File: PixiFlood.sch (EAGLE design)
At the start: 31 parts, among them IC1 78L05Z, IC2 WS2811-SOP8, IC3 TC7W04FTC7W04F, U1 PT4115PT4115B89E, U2 PT4115PT4115B89E, U3 PT4115PT4115B89E, X1 22-23-2031, X2 LED-PAD, X3 LED-PAD, X4 22-23-2031, X5 LED-PAD, X6 LED-PAD, X7 LED-PAD, X8 LED-PAD

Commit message: Reworked and retitled to PixiFlood
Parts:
- D1, D2, D3: value (none) -> 1N5819
- IC2: value WS2811-SOP8 -> WS2811SOP8; device MyLibrary:WS2811-SOP8 -> drivers:WS2811SOP8
- IC3: value TC7W04FTC7W04F -> TC7W04F; device MyLibrary:TC7W04FTC7W04F -> logic:TC7W04F
- L1, L2, L3: value SLF7045 -> 82114R; device inductors:SLF7045 -> inductors:82114R
- R1, R6: device resistor:R-US_R1206 -> resistor:R-US_0204/5
- R2, R3, R4: device rcl:R-US_M0805 -> rcl:R-US_0204/5
- R5: device resistor:R-US_M1206 -> resistor:R-US_0204/5
- U1, U2, U3: value PT4115PT4115B89E -> PT4115B89E; device IC:PT4115PT4115B89E -> drivers:PT4115B89E
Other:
- moved on the sheet: R1, R5, R6, X2, X3, X5, X6, X7, X8

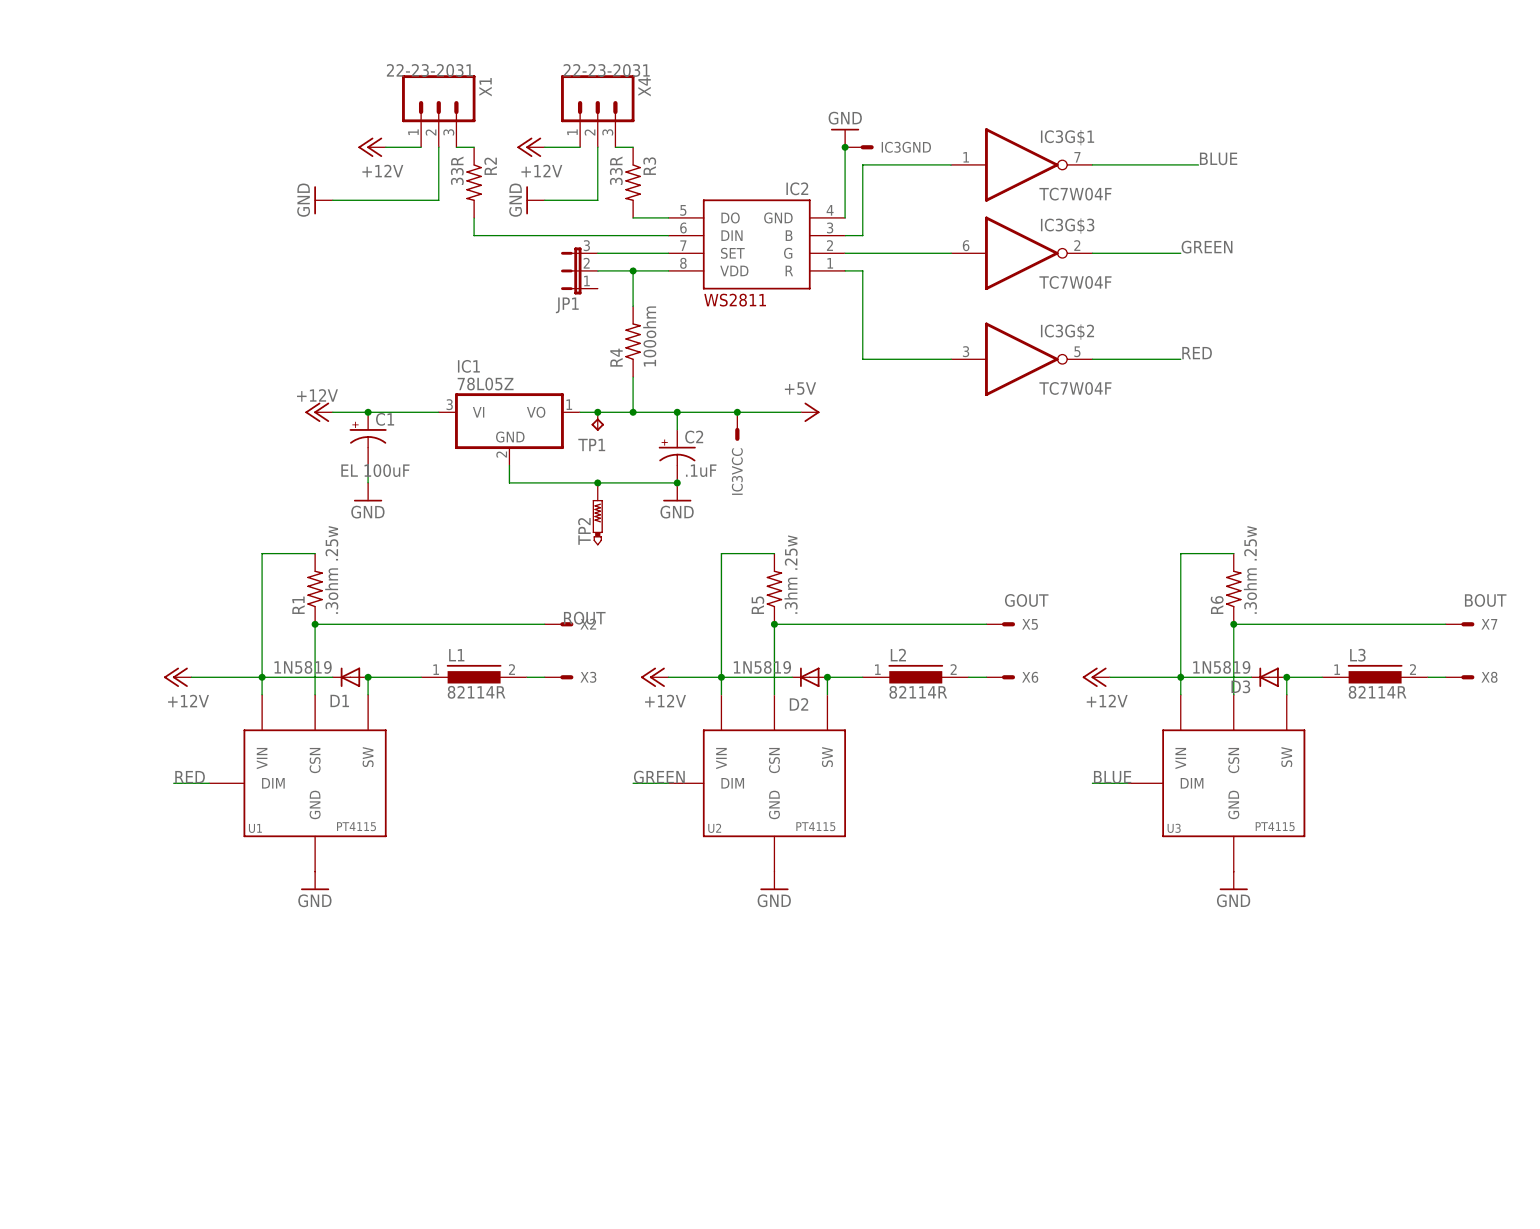
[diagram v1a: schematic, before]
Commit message: Reworked and retitled to PixiFlood SMD
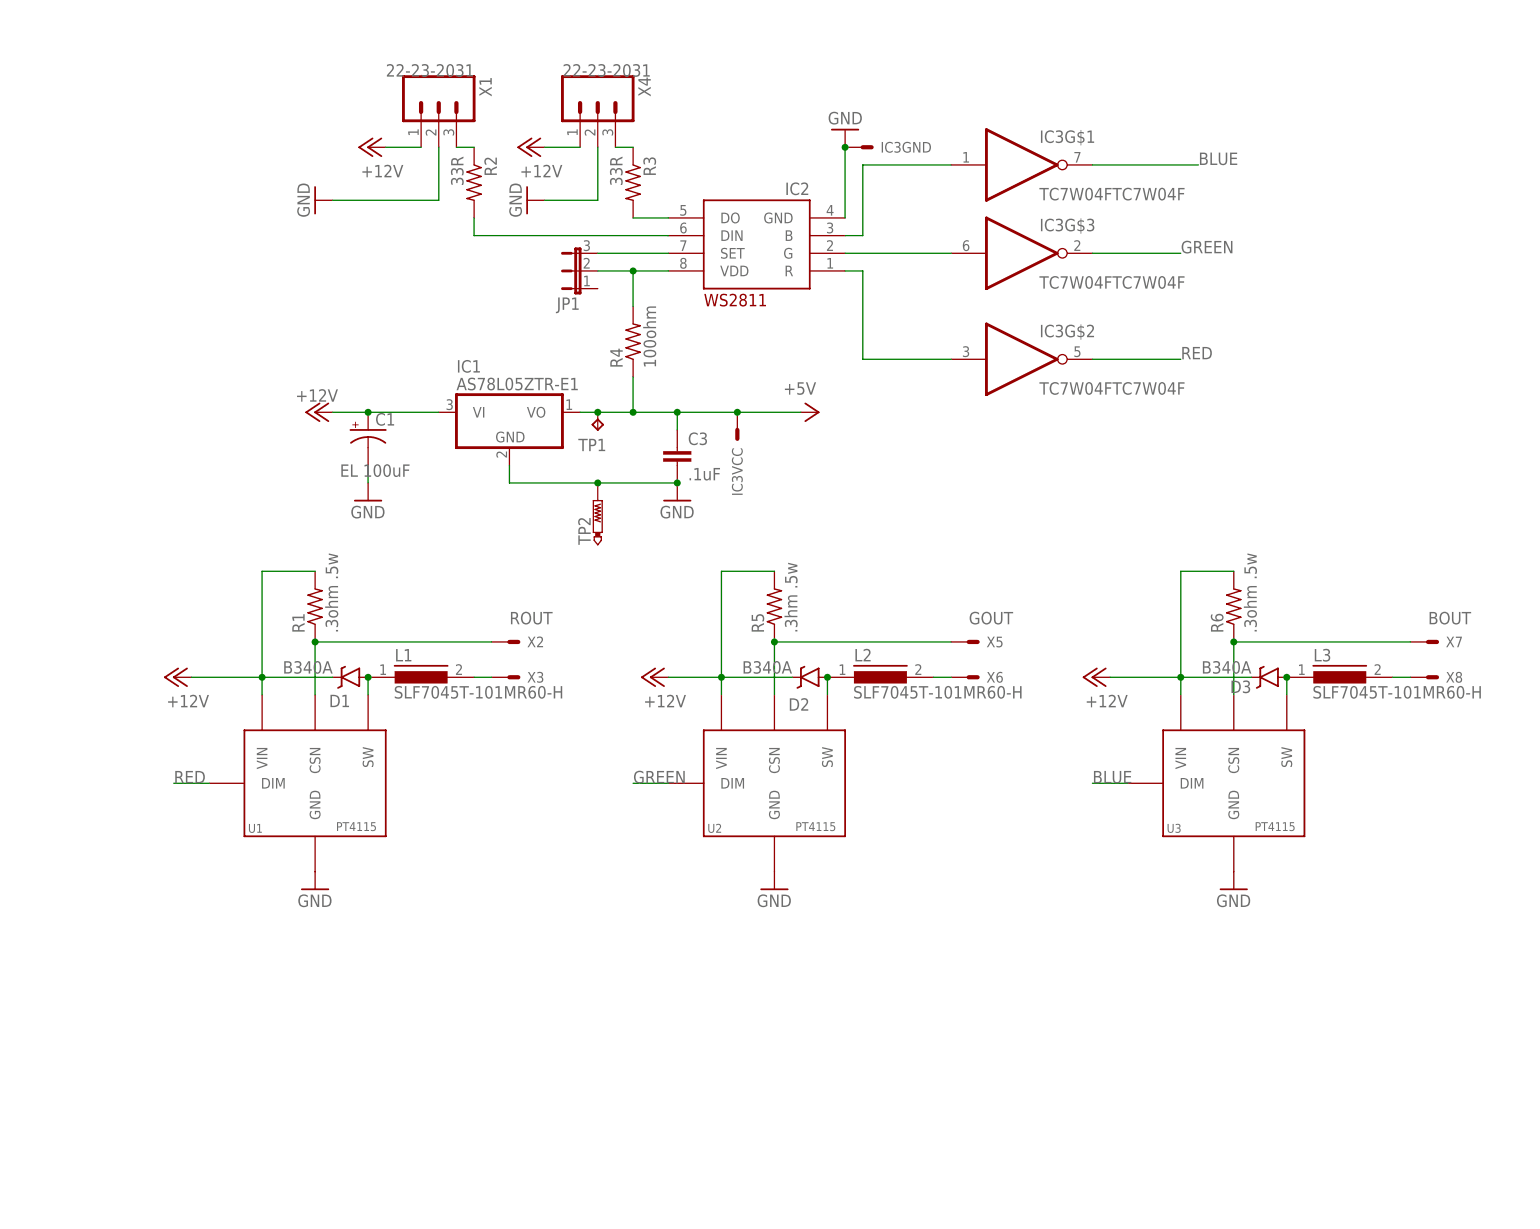
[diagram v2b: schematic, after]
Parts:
- removed C2: .1uF, resistor:CPOL-USB45181A
- added C3: .1uF, SparkFun-Capacitors:CAP1210
- D1, D2, D3: value 1N5819 -> B340A; device diode:DIODE-DO07 -> SparkFun-DiscreteSemi:DIODE-SCHOTTKY-B340A
- IC1: value 78L05Z -> AS78L05ZTR-E1
- IC2: value WS2811SOP8 -> WS2811-SOP8; device drivers:WS2811SOP8 -> MyLibrary:WS2811-SOP8
- IC3: value TC7W04F -> TC7W04FTC7W04F; device logic:TC7W04F -> MyLibrary:TC7W04FTC7W04F
- L1, L2, L3: value 82114R -> SLF7045T-101MR60-H; device inductors:82114R -> inductors:SLF7045
- R1, R6: value .3ohm .25w -> .3ohm .5w; device resistor:R-US_0204/5 -> resistor:R-US_R1210
- R2, R3, R4: device rcl:R-US_0204/5 -> rcl:R-US_R1206
- R5: value .3hm .25w -> .3hm .5w; device resistor:R-US_0204/5 -> resistor:R-US_R1210
- U1, U2, U3: value PT4115B89E -> PT4115PT4115B89E; device drivers:PT4115B89E -> IC:PT4115PT4115B89E
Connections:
- net +5V: now also C3.1; no longer C2.+
- net GND: now also C3.2; no longer C2.-
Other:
- moved on the sheet: R1, R5, R6, X2, X3, X5, X6, X7, X8

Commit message: Reworked layout
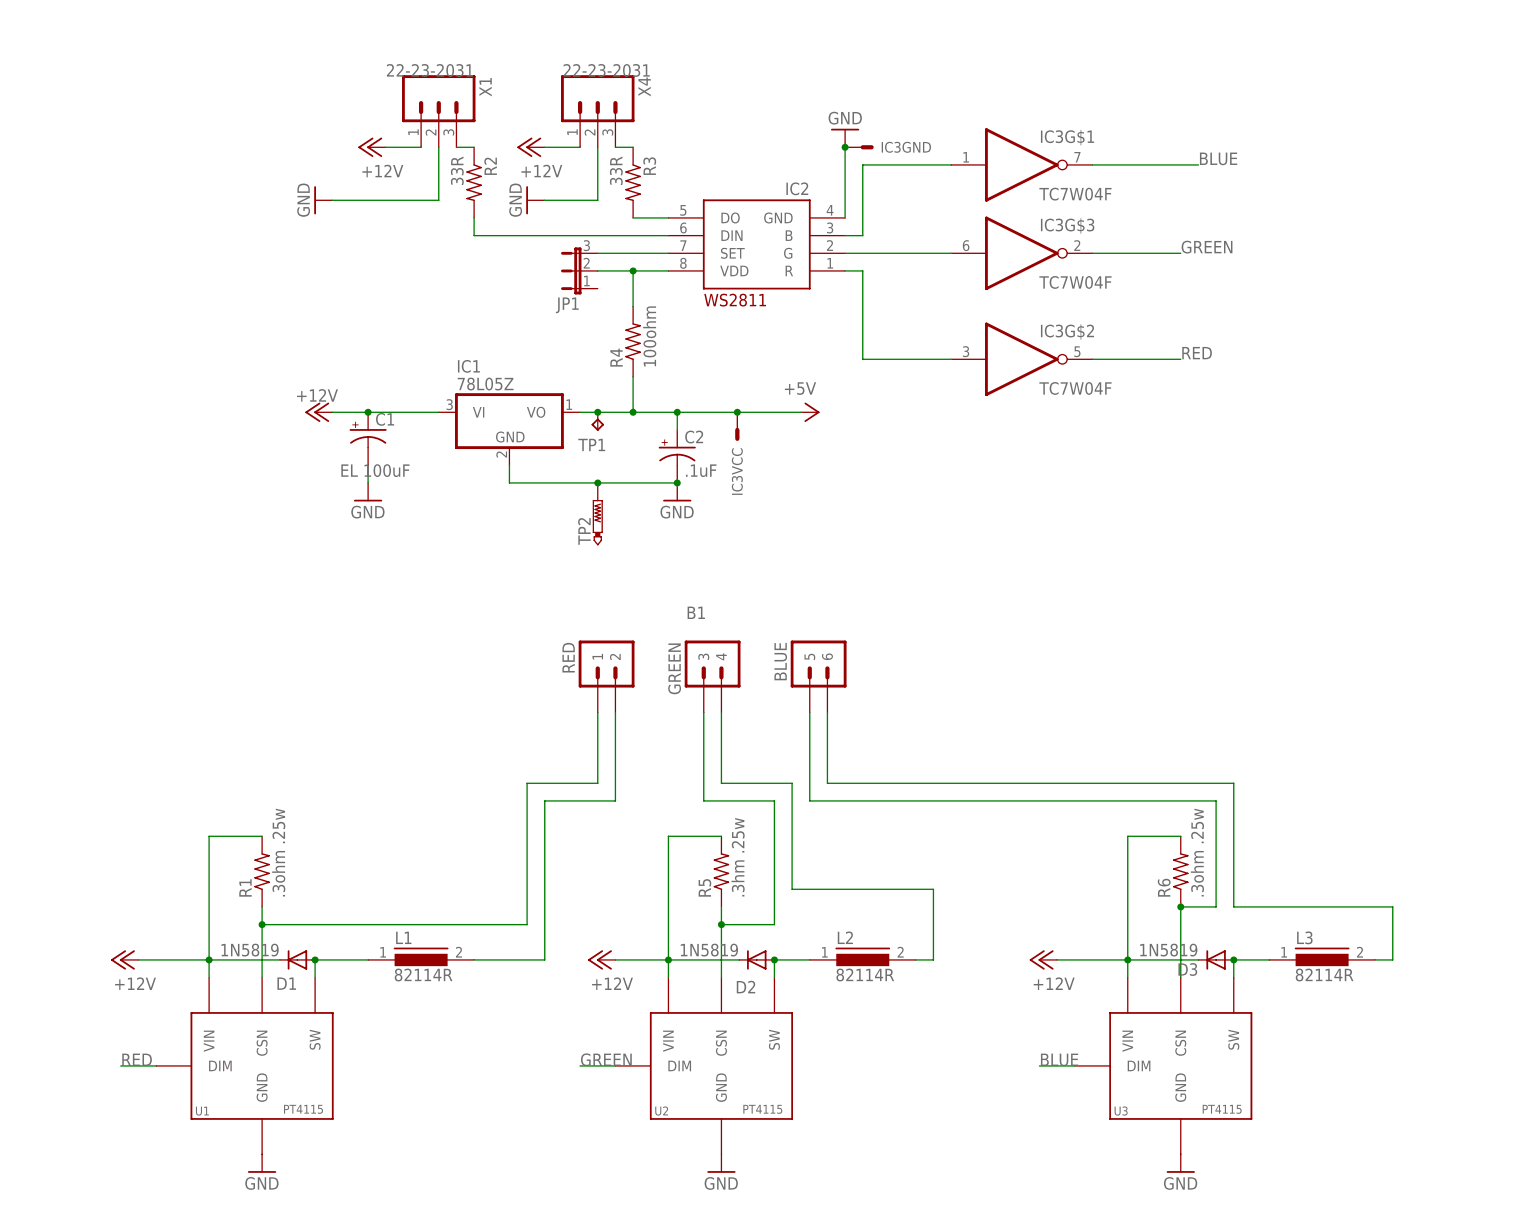
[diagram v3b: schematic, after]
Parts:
- removed C3: .1uF, SparkFun-Capacitors:CAP1210
- removed X2, X3, X5, X6, X7, X8: LED-PAD, MyLibrary:LED-PAD
- added B1: LED-BOARDV2, special:LED-BOARDV2
- added C2: .1uF, resistor:CPOL-USB45181A
- D1, D2, D3: value B340A -> 1N5819; device SparkFun-DiscreteSemi:DIODE-SCHOTTKY-B340A -> diode:DIODE-DO07
- IC1: value AS78L05ZTR-E1 -> 78L05Z
- IC2: value WS2811-SOP8 -> WS2811SOP8; device MyLibrary:WS2811-SOP8 -> drivers:WS2811SOP8
- IC3: value TC7W04FTC7W04F -> TC7W04F; device MyLibrary:TC7W04FTC7W04F -> logic:TC7W04F
- L1, L2, L3: value SLF7045T-101MR60-H -> 82114R; device inductors:SLF7045 -> inductors:82114R
- R1, R6: value .3ohm .5w -> .3ohm .25w; device resistor:R-US_R1210 -> resistor:R-US_0204/5
- R2, R3, R4: device rcl:R-US_R1206 -> rcl:R-US_0204/5
- R5: value .3hm .5w -> .3hm .25w; device resistor:R-US_R1210 -> resistor:R-US_0204/5
- U1, U2, U3: value PT4115PT4115B89E -> PT4115B89E; device IC:PT4115PT4115B89E -> drivers:PT4115B89E
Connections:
- net +5V: now also C2.+; no longer C3.1
- net BOUT: now also B1.5; no longer X7.S
- net GND: now also C2.-; no longer C3.2
- net GOUT: now also B1.3; no longer X5.S
- net N$10: now also B1.6; no longer X8.S
- net N$3: now also B1.2; no longer X3.S
- net N$9: now also B1.4; no longer X6.S
- net ROUT: now also B1.1; no longer X2.S
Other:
- moved on the sheet: R1, R5, R6, U1, U2, U3

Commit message: Reworked layout
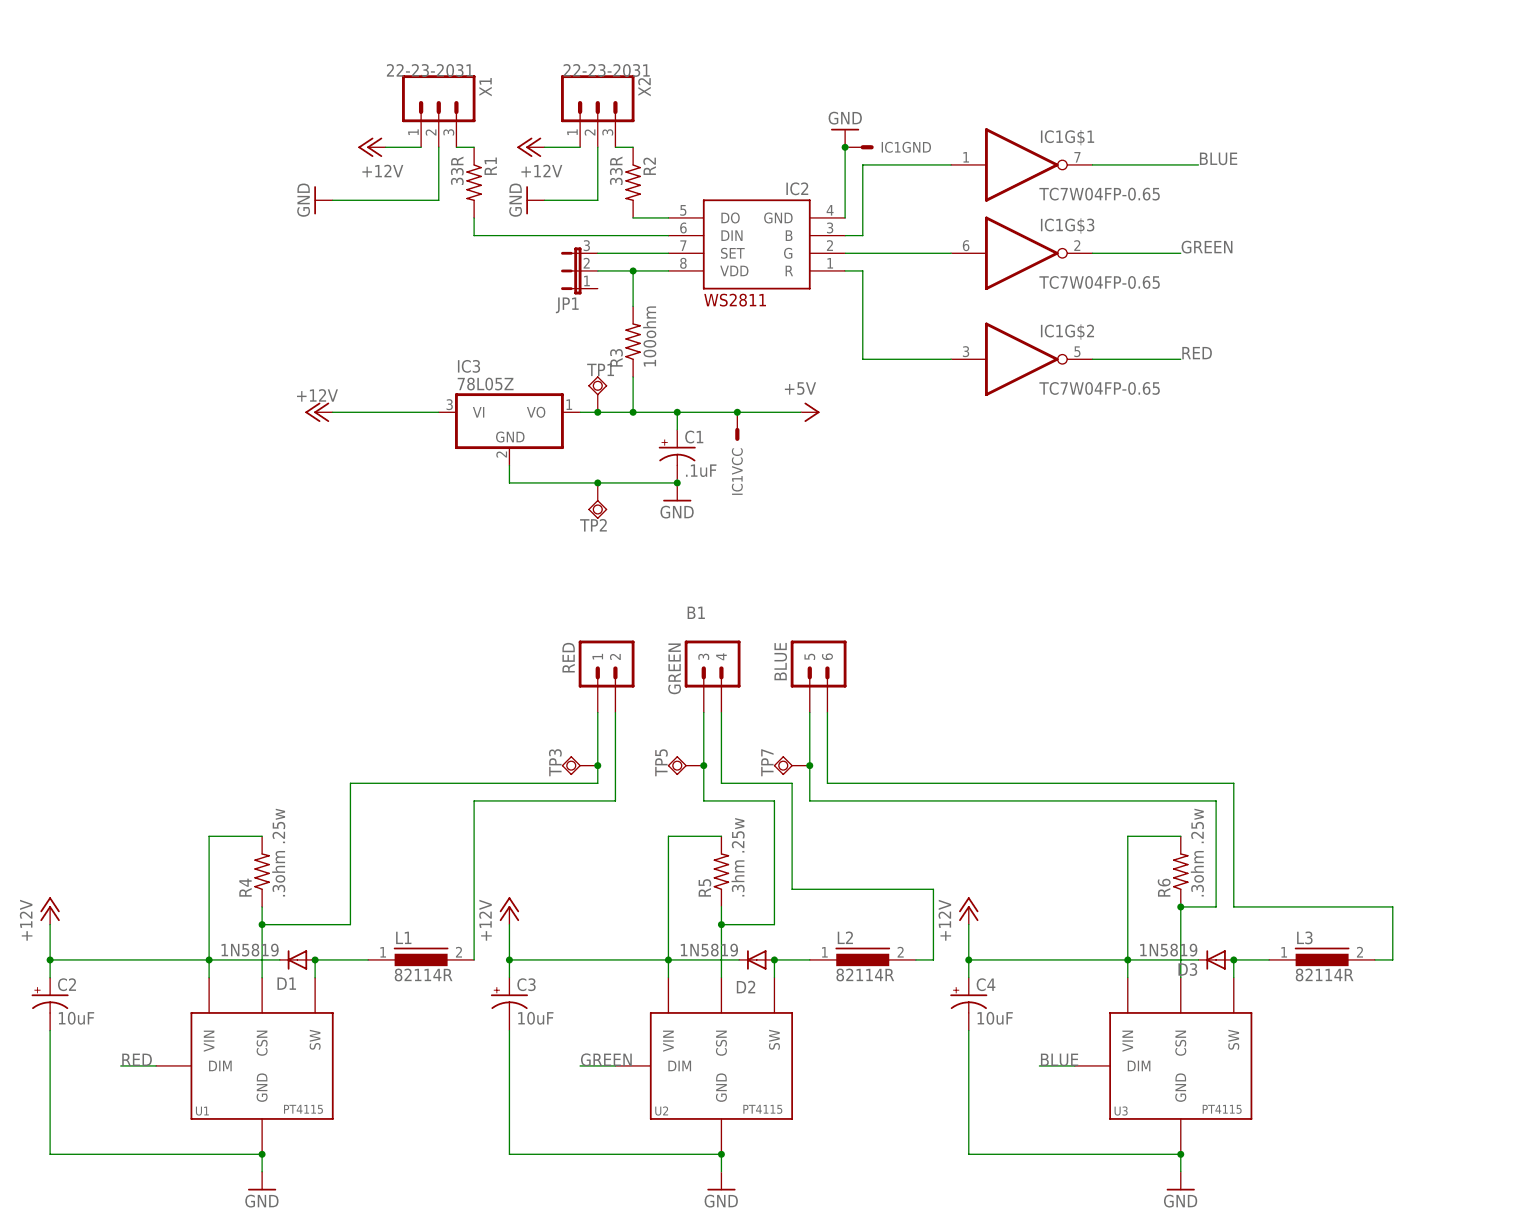
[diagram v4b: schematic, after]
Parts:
- added C3, C4: 10uF, adafruit:CPOL-USE2.5-5
- added TP3, TP5, TP7: TPSQTP15R, testpad:TPSQTP15R
- C1: value EL 100uF -> .1uF; device rcl:CPOL-USTT2D6L -> capacitors:CAP_POLPTH50
- C2: value .1uF -> 10uF; device resistor:CPOL-USB45181A -> adafruit:CPOL-USE2.5-5
- IC1: value 78L05Z -> TC7W04FP-0.65; device linear:78L05Z -> logic:TC7W04FP-0.65
- IC3: value TC7W04F -> 78L05Z; device logic:TC7W04F -> linear:78L05Z
- R1: value .3ohm .25w -> 33R; device resistor:R-US_0204/5 -> rcl:R-US_0204/5
- R3: value 33R -> 100ohm
- R4: value 100ohm -> .3ohm .25w; device rcl:R-US_0204/5 -> resistor:R-US_0204/5
- TP1: value TPB2,54 -> TPSQTP20R; device testpad:TPB2,54 -> testpad:TPSQTP20R
- TP2: value PTR1TP20SQ -> TPSQTP20SQ; device testpad:PTR1TP20SQ -> testpad:TPSQTP20SQ
- renumbered X4 to X2
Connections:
- net +12V: now also C2.+, C3.+, C4.+, IC3.VI, R4.2; no longer C1.+, IC1.VI, R1.2
- net +5V: now also C1.+, IC1VCC.S, IC3.VO, R3.1; no longer C2.+, IC1.VO, IC3VCC.S, R4.1
- net BLUE: now also IC1G$1.O; no longer IC3G$1.O
- net BOUT: now also TP7.TP
- net GND: now also C3.-, C4.-, IC1GND.S, IC3.GND; no longer IC1.GND, IC3GND.S
- net GOUT: now also TP5.TP
- net GREEN: now also IC1G$3.O; no longer IC3G$3.O
- net N$14: now also R3.2; no longer R4.2
- net N$15: now also IC1G$2.I; no longer IC3G$2.I
- net N$16: now also IC1G$1.I; no longer IC3G$1.I
- net N$19: now also IC1G$3.I; no longer IC3G$3.I
- net N$4: now also R2.1; no longer R3.1
- net N$6: now also R1.1; no longer R2.1
- net N$7: now also R2.2; no longer R3.2
- net N$8: now also R1.2; no longer R2.2
- net RED: now also IC1G$2.O; no longer IC3G$2.O
- net ROUT: now also R4.1, TP3.TP; no longer R1.1
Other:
- moved on the sheet: C1, C2, R1, R2, R3, R4
